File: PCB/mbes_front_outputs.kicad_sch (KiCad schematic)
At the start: 61 parts, among them Q1 BC807, Q10 BC817, Q11 BC817, Q12 TPCA8120,L1Q, Q13 BC817, Q14 BC817, Q15 BC817, Q16 TPCA8120,L1Q, Q17 BC817, Q18 TPCA8120,L1Q, Q20 BC807, Q21 BC807, Q5 TPCA8120,L1Q, Q6 TPCA8120,L1Q, Q7 TPCA8120,L1Q, Q8 BC817, Q9 BC817

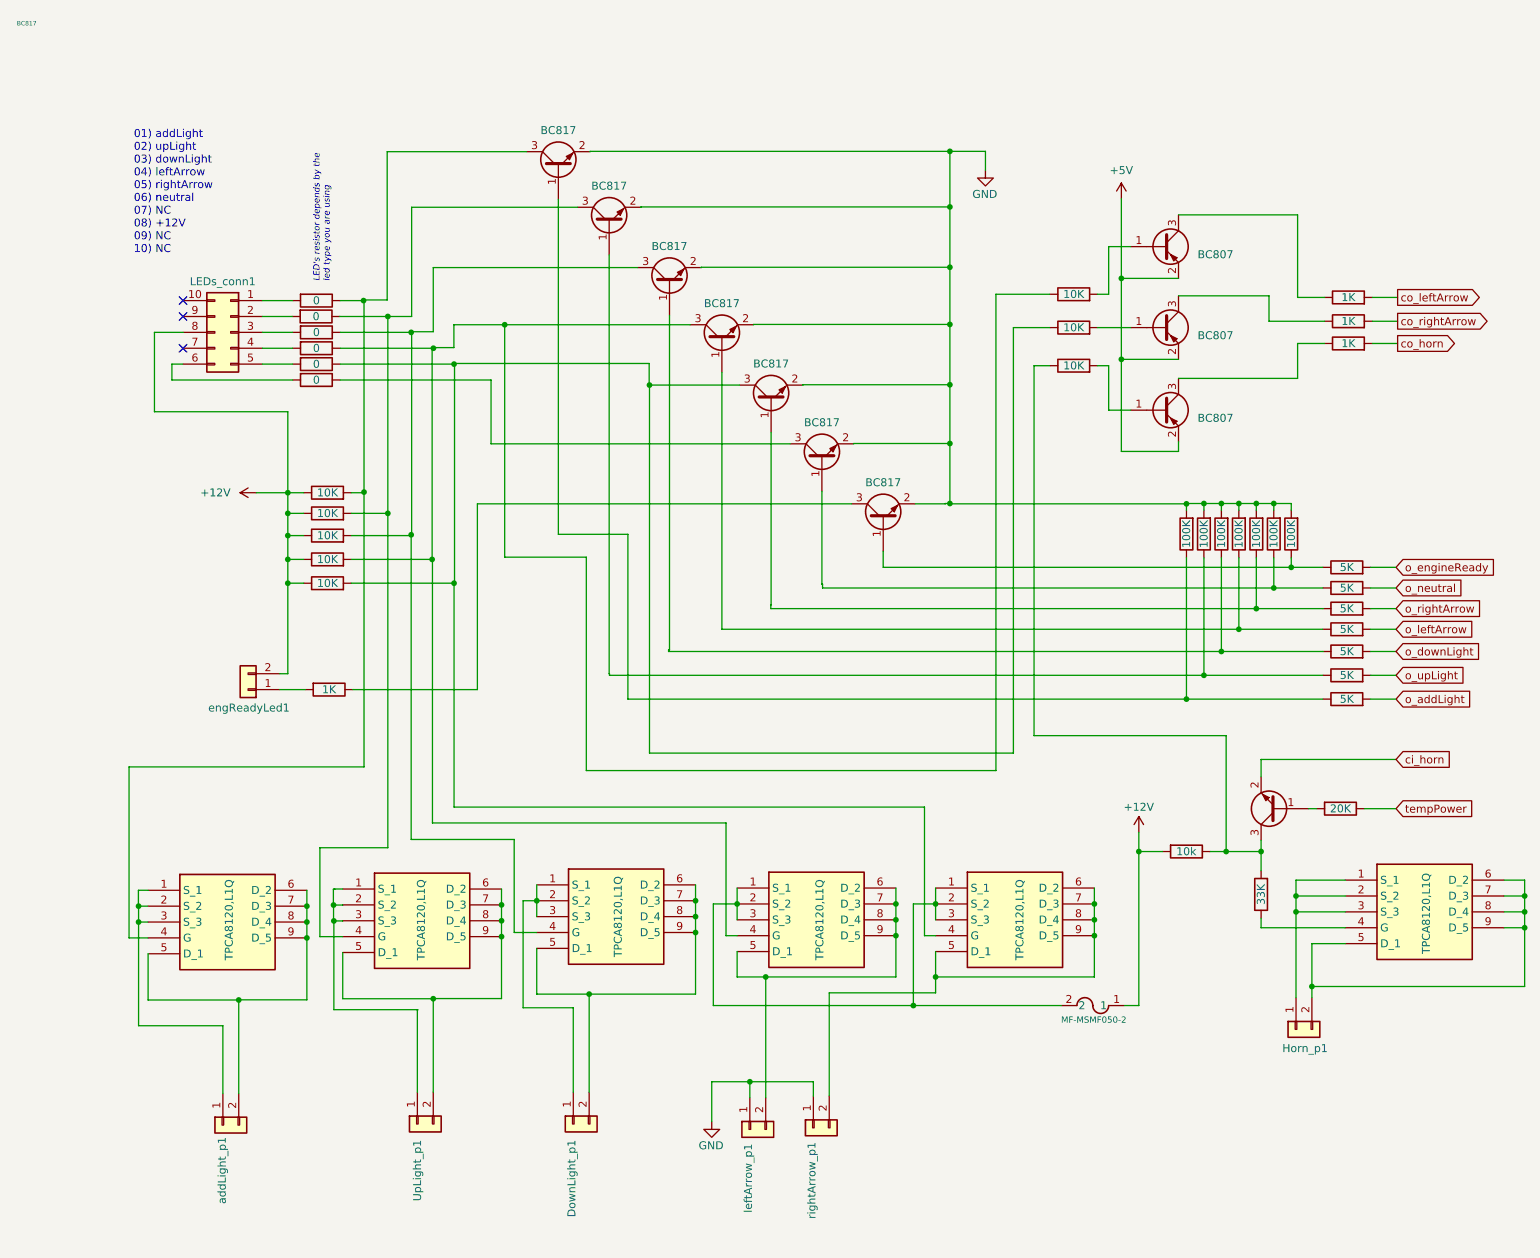
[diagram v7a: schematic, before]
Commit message: Merge from ESP32__dualPCB branch
- DownLight: external fuse replaced by internal automatic one, wire connector replaced by 2.54 pin-header
- The resistor between FET's gate and NPN's collector has been removed
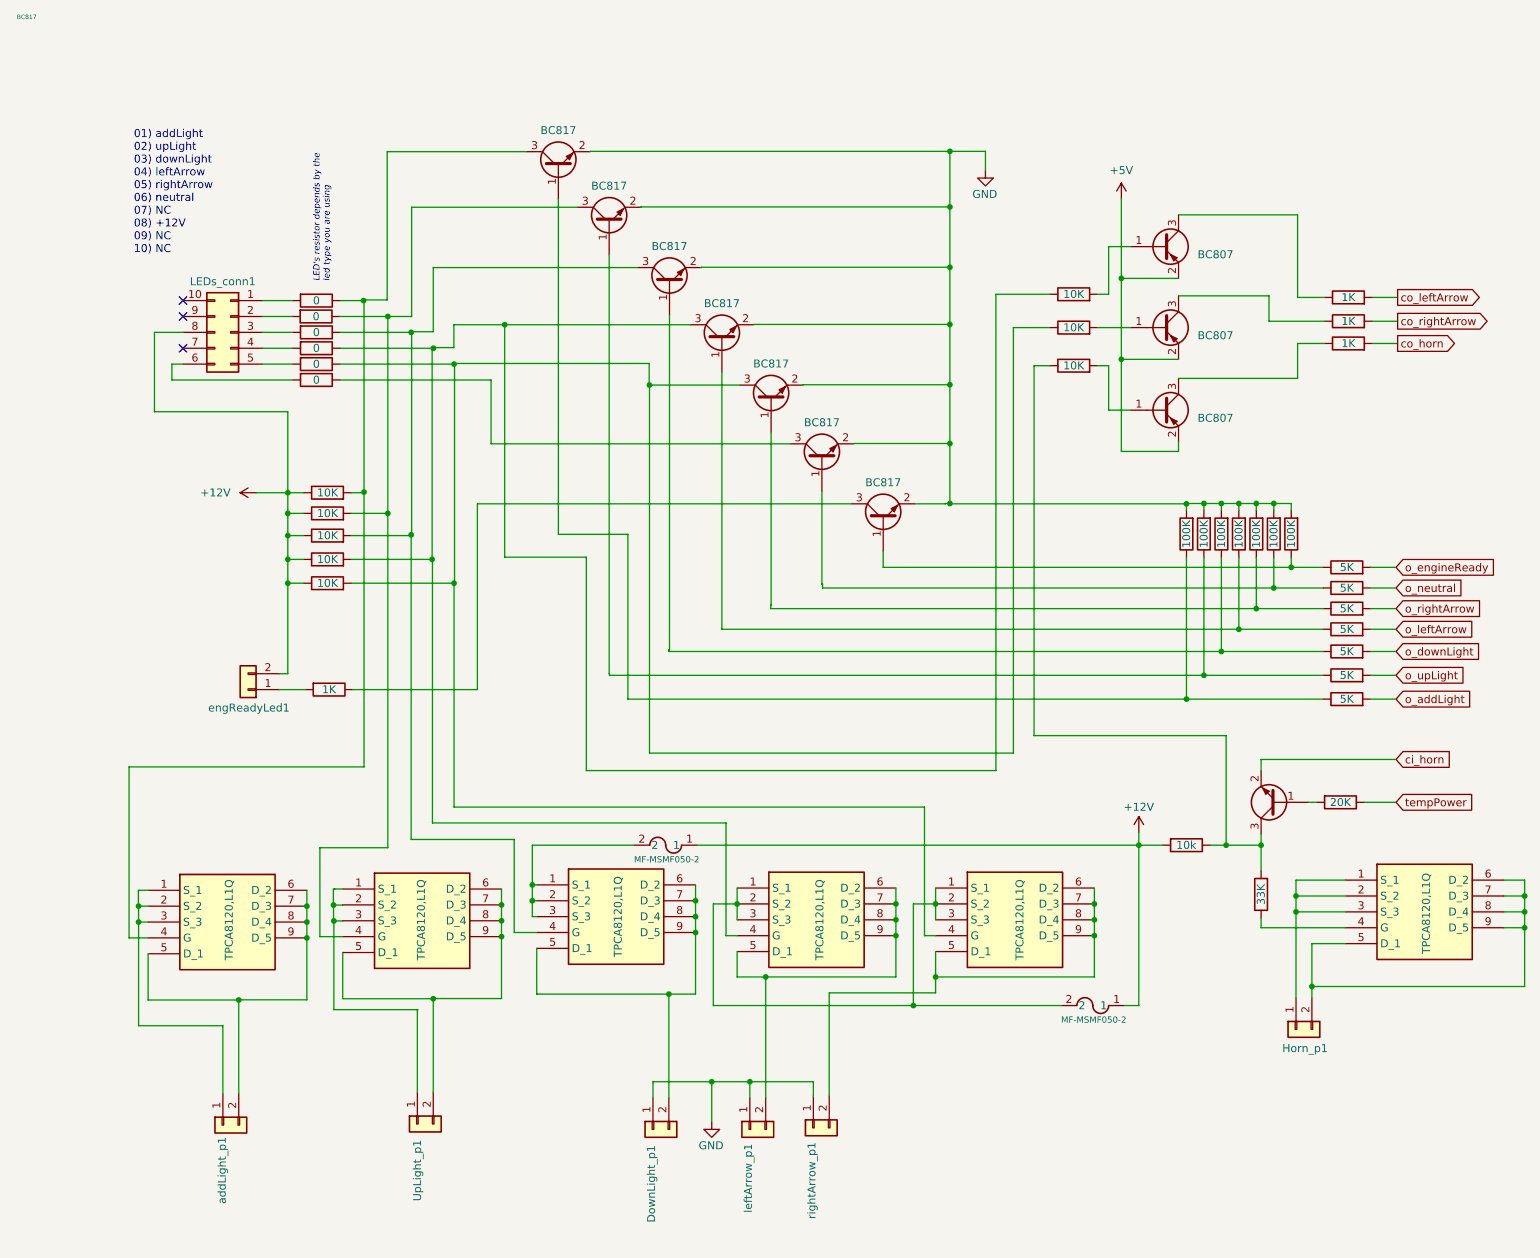
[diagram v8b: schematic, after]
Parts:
- added F2: MF-MSMF050-2, MSMF:FUSE_F050-2, symbol MSMF050-2:MF-MSMF050-2
- DownLight_p1: footprint Connector_Wire:SolderWire-1sqmm_1x02_P5.4mm_D1.4mm_OD2.7mm -> Connector_PinHeader_2.54mm:PinHeader_1x02_P2.54mm_Vertical
- F1: footprint MF-MSMF050-2:FUSE_F050-2 -> MSMF:FUSE_F050-2
- leftArrow_p1, rightArrow_p1: footprint Connector_Wire:SolderWire-0.75sqmm_1x02_P4.8mm_D1.25mm_OD2.3mm -> Connector_PinHeader_2.54mm:PinHeader_1x02_P2.54mm_Vertical
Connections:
- net +12V: now also F2.1
- net GND: now also DownLight_p1.1 (Pin_1)
- net at Q7.1 (S_1), Q7.2 (S_2), Q7.3 (S_3): now also F2.2; no longer DownLight_p1.1 (Pin_1)
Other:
- company: (none) -> https://github.com/catinella/mbElectricalSystem
- title: (none) -> (front side) Motorbike Electrical System
- moved on the sheet: DownLight_p1
